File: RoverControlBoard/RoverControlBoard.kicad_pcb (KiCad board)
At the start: 2 copper layers, 38 x 92 mm, 20 parts, among them P1 CONN_01X03, P10 CONN_01X02, P11 CONN_01X02, P12 CONN_01X03, P2 CONN_01X03, P4 CONN_01X03, P5 CONN_01X03, P7 CONN_01X05, P9 CONN_01X02, Q1 Q_NMOS_GDS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

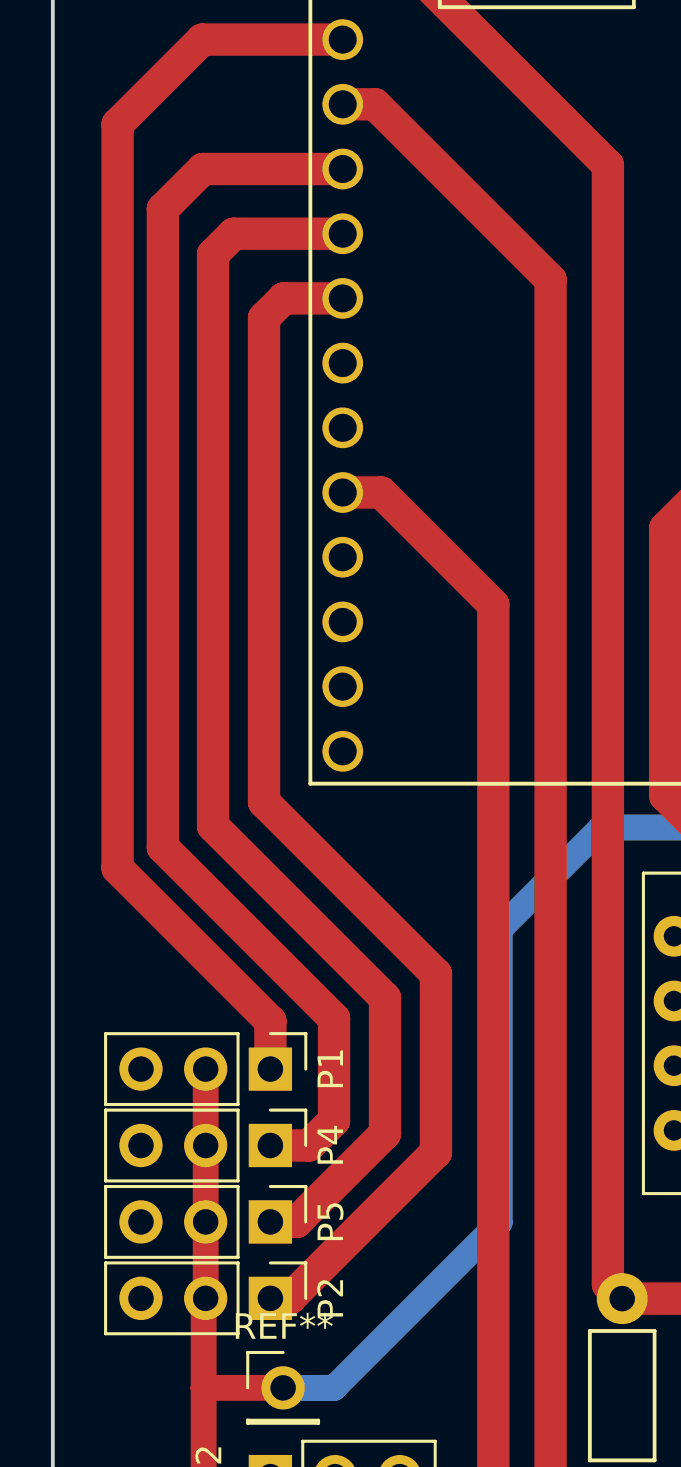
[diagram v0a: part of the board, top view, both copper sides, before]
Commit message: changes track spacing on board for better etching in the future
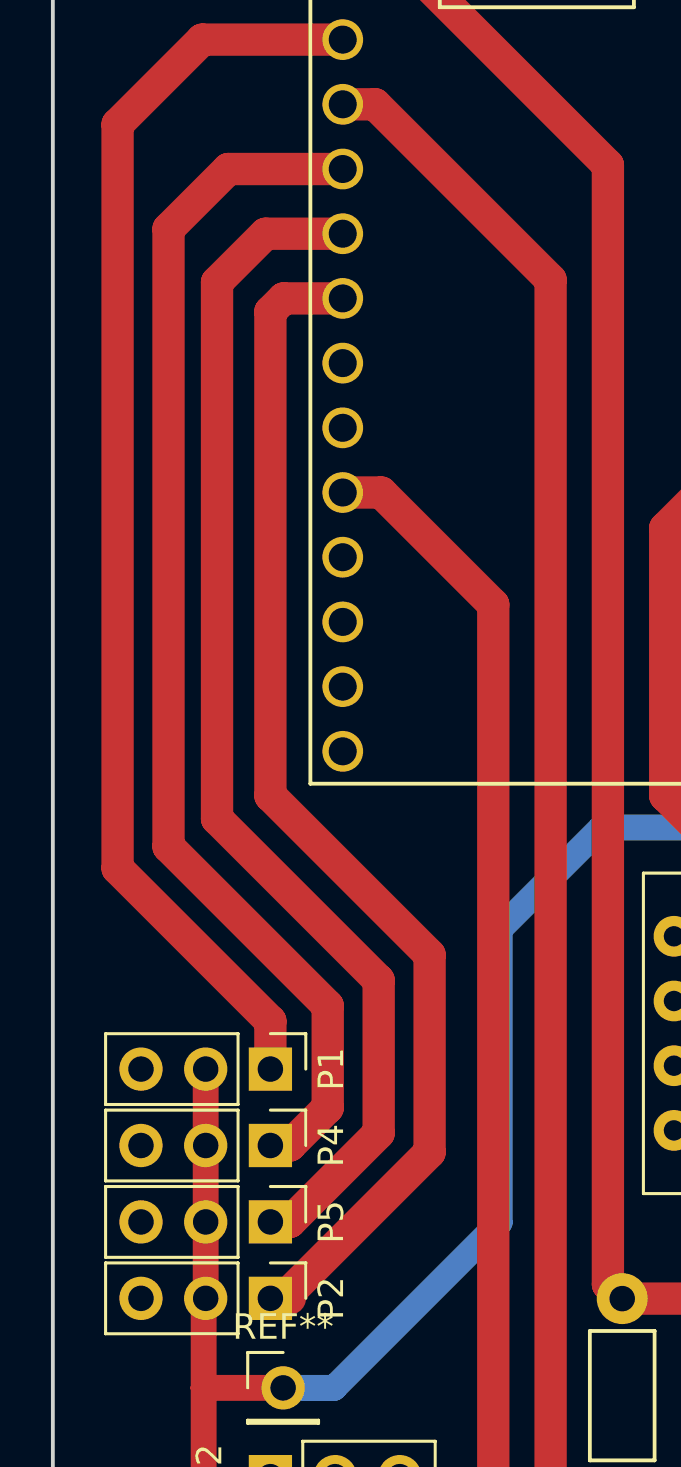
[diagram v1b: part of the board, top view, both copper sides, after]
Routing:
- net /PanServo: track 49.2 -> 47.8 mm
- net /TiltServo: track 48.7 -> 47.5 mm
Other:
- net class Large: clearance 0.508 -> 0.635; via_dia 0.6858 -> 1.27
- net class Medium: clearance 0.381 -> 0.635; via_dia 3 -> 0.762; via_drill 1 -> 0.3302
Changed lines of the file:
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@@
     (thickness 1.6)
     (drawings 14)
-    (tracks 104)
+    (tracks 105)
     (zones 0)
     (modules 20)
     (nets 23)
   )
-  (page USLetter)
+  (page User 266.7 184.15)
   (title_block
     (title "SealCam - Rover Control Board")
@@
   )
   (net_class Large ""
-    (clearance 0.508)
+    (clearance 0.635)
     (trace_width 1.27)
-    (via_dia 0.6858)
+    (via_dia 1.27)
     (via_drill 0.3302)
     (uvia_dia 0.2032)
@@
   )
   (net_class Medium ""
-    (clearance 0.381)
+    (clearance 0.635)
     (trace_width 0.635)
-    (via_dia 3)
-    (via_drill 1)
+    (via_dia 0.762)
+    (via_drill 0.3302)
     (uvia_dia 0.2032)
     (uvia_drill 0.1016)
@@
   (segment (start 130.46 91.985) (end 130.46 88.985) (width 1.016) (layer F.Cu) (net 2))
   (segment (start 130.46 88.985) (end 130.46 85.985) (width 1.016) (layer F.Cu) (net 2))
+  (segment (start 133 94.985) (end 133.515 94.985) (width 1.27) (layer F.Cu) (net 4))
+  (segment (start 133.515 94.985) (end 139.25 89.25) (width 1.27) (layer F.Cu) (net 4))
+  (segment (start 133.52 55.73) (end 135.84 55.73) (width 1.27) (layer F.Cu) (net 4))
+  (segment (start 133 56.25) (end 133.52 55.73) (width 1.27) (layer F.Cu) (net 4))
+  (segment (start 133 75.25) (end 133 56.25) (width 1.27) (layer F.Cu) (net 4))
+  (segment (start 139.25 81.5) (end 133 75.25) (width 1.27) (layer F.Cu) (net 4))
+  (segment (start 139.25 89.25) (end 139.25 81.5) (width 1.27) (layer F.Cu) (net 4))
   (segment (start 133 94.985) (end 133.765 94.985) (width 1.27) (layer F.Cu) (net 4))
-  (segment (start 133.765 94.985) (end 139.5 89.25) (width 1.27) (layer F.Cu) (net 4))
-  (segment (start 139.5 89.25) (end 139.5 82.25) (width 1.27) (layer F.Cu) (net 4))
-  (segment (start 139.5 82.25) (end 132.75 75.5) (width 1.27) (layer F.Cu) (net 4))
-  (segment (start 132.75 75.5) (end 132.75 56.5) (width 1.27) (layer F.Cu) (net 4))
-  (segment (start 132.75 56.5) (end 133.52 55.73) (width 1.27) (layer F.Cu) (net 4))
-  (segment (start 133.52 55.73) (end 135.84 55.73) (width 1.27) (layer F.Cu) (net 4))
-  (segment (start 133 88.985) (end 134.515 88.985) (width 1.27) (layer F.Cu) (net 5))
-  (segment (start 130.35 50.65) (end 135.84 50.65) (width 1.27) (layer F.Cu) (net 5))
-  (segment (start 128.778002 52.221998) (end 130.35 50.65) (width 1.27) (layer F.Cu) (net 5))
-  (segment (start 128.778002 77.278002) (end 128.778002 52.221998) (width 1.27) (layer F.Cu) (net 5))
-  (segment (start 135.5 84) (end 128.778002 77.278002) (width 1.27) (layer F.Cu) (net 5))
-  (segment (start 135.5 88) (end 135.5 84) (width 1.27) (layer F.Cu) (net 5))
-  (segment (start 134.515 88.985) (end 135.5 88) (width 1.27) (layer F.Cu) (net 5))
-  (segment (start 133 91.985) (end 134.029474 91.985) (width 1.27) (layer F.Cu) (net 6))
-  (segment (start 131.56 53.19) (end 135.84 53.19) (width 1.27) (layer F.Cu) (net 6))
-  (segment (start 130.75 54) (end 131.56 53.19) (width 1.27) (layer F.Cu) (net 6))
-  (segment (start 130.75 76.443996) (end 130.75 54) (width 1.27) (layer F.Cu) (net 6))
-  (segment (start 137.5 83.193996) (end 130.75 76.443996) (width 1.27) (layer F.Cu) (net 6))
-  (segment (start 137.5 88.514474) (end 137.5 83.193996) (width 1.27) (layer F.Cu) (net 6))
-  (segment (start 134.029474 91.985) (end 137.5 88.514474) (width 1.27) (layer F.Cu) (net 6))
+  (segment (start 133 88.985) (end 133.765 88.985) (width 1.27) (layer F.Cu) (net 5))
+  (segment (start 133.765 88.985) (end 135.25 87.5) (width 1.27) (layer F.Cu) (net 5))
+  (segment (start 135.25 87.5) (end 135.25 83.5) (width 1.27) (layer F.Cu) (net 5))
+  (segment (start 135.25 83.5) (end 129 77.25) (width 1.27) (layer F.Cu) (net 5))
+  (segment (start 129 77.25) (end 129 53) (width 1.27) (layer F.Cu) (net 5))
+  (segment (start 129 53) (end 131.35 50.65) (width 1.27) (layer F.Cu) (net 5))
+  (segment (start 131.35 50.65) (end 135.84 50.65) (width 1.27) (layer F.Cu) (net 5))
+  (segment (start 133 91.985) (end 133.765 91.985) (width 1.27) (layer F.Cu) (net 6))
+  (segment (start 133.765 91.985) (end 137.25 88.5) (width 1.27) (layer F.Cu) (net 6))
+  (segment (start 137.25 88.5) (end 137.25 82.5) (width 1.27) (layer F.Cu) (net 6))
+  (segment (start 137.25 82.5) (end 130.905002 76.155002) (width 1.27) (layer F.Cu) (net 6))
+  (segment (start 130.905002 76.155002) (end 130.905002 55.094998) (width 1.27) (layer F.Cu) (net 6))
+  (segment (start 130.905002 55.094998) (end 132.81 53.19) (width 1.27) (layer F.Cu) (net 6))
+  (segment (start 132.81 53.19) (end 135.84 53.19) (width 1.27) (layer F.Cu) (net 6))
   (segment (start 138.08 101.985) (end 138.08 106.905) (width 1.016) (layer F.Cu) (net 7))
   (segment (start 138.08 106.905) (end 138 106.985) (width 1.016) (layer F.Cu) (net 7))

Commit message: changed drill holes to reflect 3/64 drill available and adapted annular rings to leave more copper for soldering. Also increased pour isolation for better etching.
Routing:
- net /SBUS: track 49.8 -> 47.1 mm
- net /PanServo: track 47.8 -> 46.9 mm
- net /TiltServo: track 47.5 -> 48.2 mm
- net /Throttle: track 48.0 -> 48.6 mm
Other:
- board size 38 x 92 mm -> 40 x 92 mm
- net class Default: via_dia 3 -> 1.5494; via_drill 1 -> 1.190625
- net class Large: via_dia 1.27 -> 1.778; via_drill 0.3302 -> 1.190625
- net class Medium: via_dia 0.762 -> 1.5494; via_drill 0.3302 -> 1.190625
- rule via_min_drill: 0.3302 -> 1.190625
- rule via_min_size: 0.6858 -> 1.524

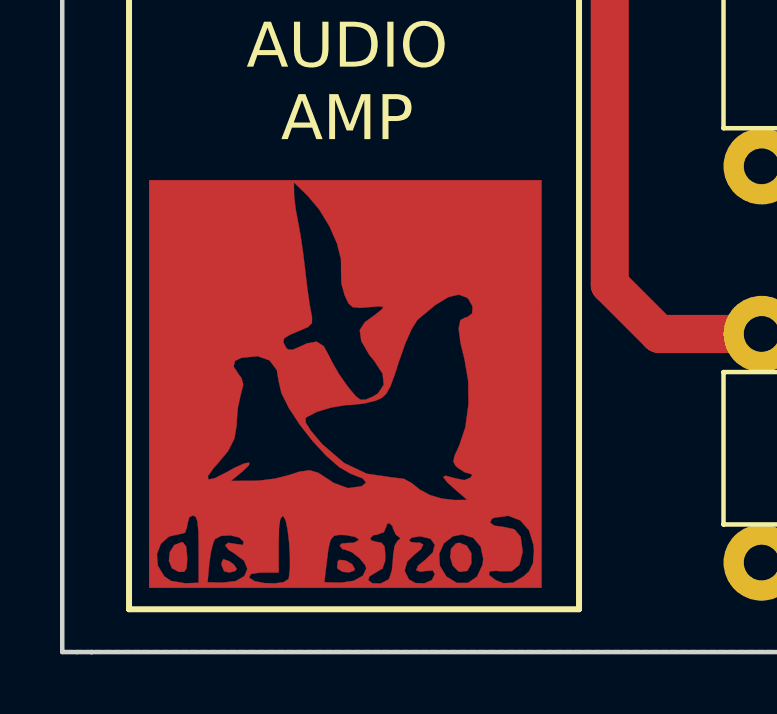
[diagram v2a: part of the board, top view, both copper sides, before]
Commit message: modified firmware to reflect harware switch order
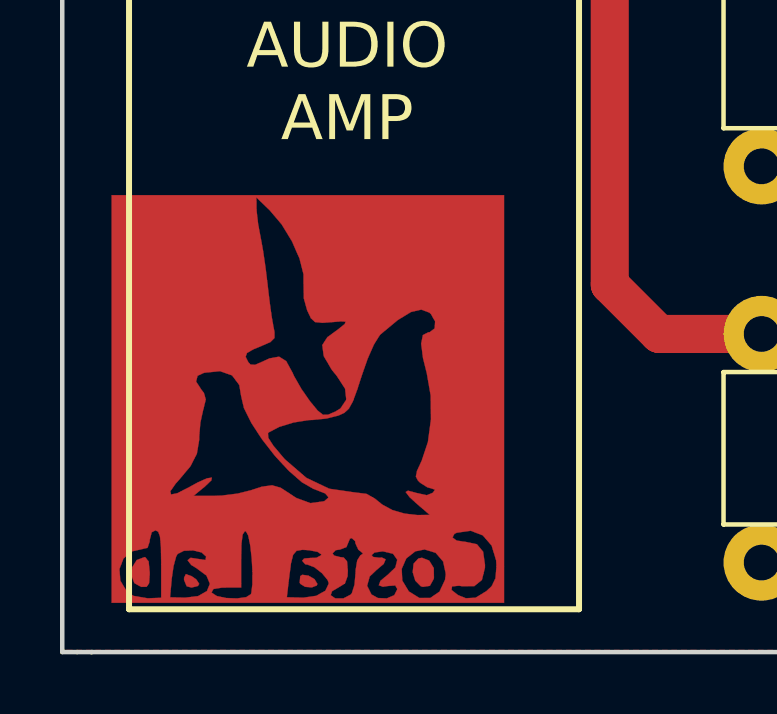
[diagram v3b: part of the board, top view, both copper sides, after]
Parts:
- moved G*** 1.35 mm to (131.8, 122.5)
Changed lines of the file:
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@@
     (links 42)
     (no_connects 0)
-    (area 117.789999 31.15 177 132.0518)
+    (area 117.789999 32.65 177 132.0518)
     (thickness 1.6)
     (drawings 18)
@@
   )
   (module Logos:CostaLab_SmallCopper_mirrored (layer F.Cu)
-    (at 133 122)
+    (at 131.75 122.5)
     (fp_text reference G*** (at -4.1 8) (layer F.SilkS) hide
       (effects (font (thickness 0.3)))
